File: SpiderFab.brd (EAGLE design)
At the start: 69.8 x 50.8 mm, 47 parts, among them IC1 SN754410, J14 5.5x2.1mm Barrel, U1 ATMEGA328, U3 MCP73831, X1 USBSMD, Y1 16MHz

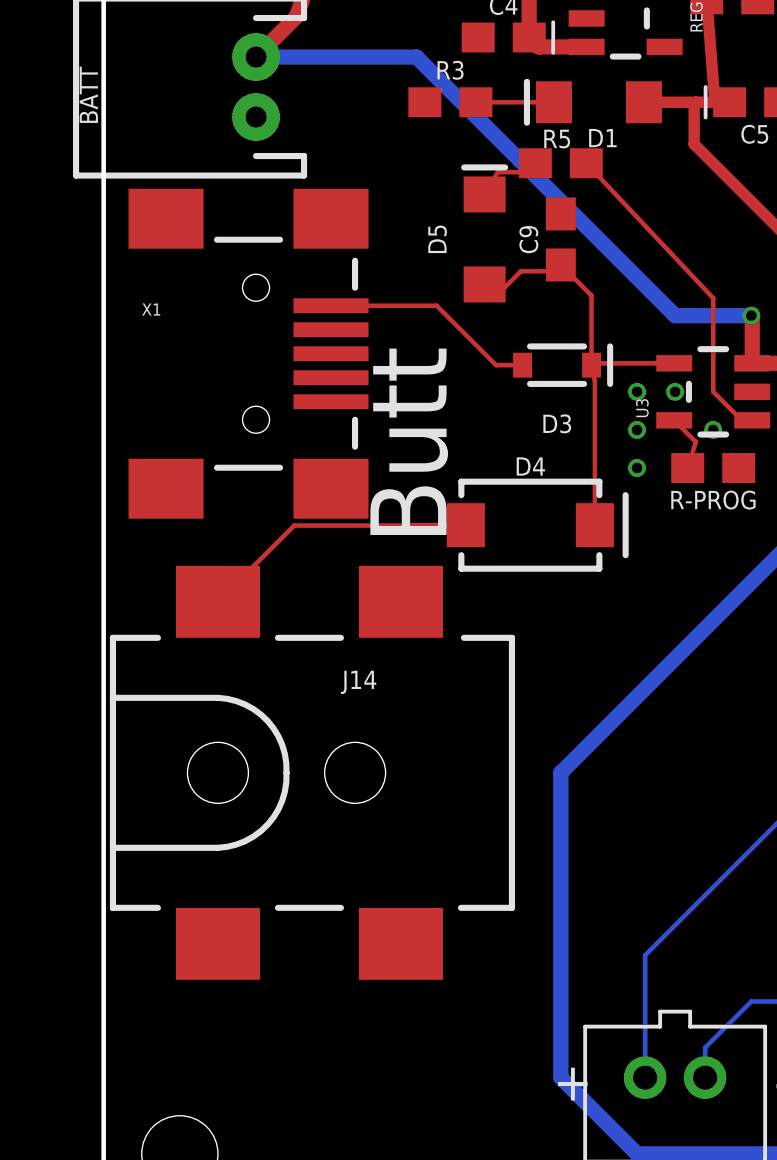
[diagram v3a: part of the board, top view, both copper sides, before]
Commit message: Swap some components for a different package.
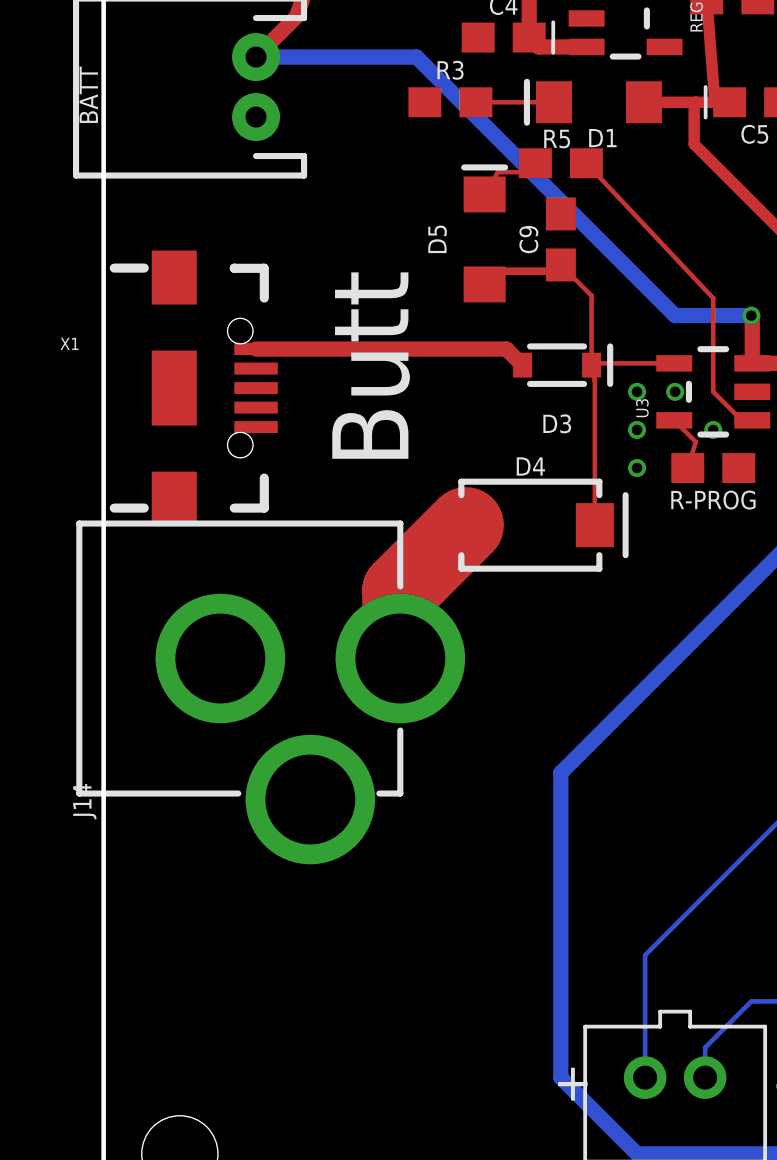
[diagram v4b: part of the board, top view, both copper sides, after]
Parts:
- J14: value 5.5x2.1mm Barrel -> POWER_JACK; device SparkFun-Connectors:POWER_JACK_SMD -> SparkFun-Connectors:POWER_JACK_PTH
- X1: value USBSMD -> AMP FCI 10103594-0001LF; device SparkFun-Connectors:USB-MINIB -> SparkFun-Connectors:USB-B-MICRO-SMD
- moved J14 8.52 mm to (-3.81, 19.1), turned to 270 degrees
- moved X1 2.96 mm to (2.35, 28.1)
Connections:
- net GND: now also J14.GNDBREAK; no longer J14.P$4
- net N$9: now also J14.PWR; no longer J14.VIN0
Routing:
- net N$9: track 9.32 -> 5.35 mm
- net N$8: track 7.20 -> 9.11 mm
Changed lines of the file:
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@@
 <wire x1="65.405" y1="40.64" x2="53.34" y2="40.64" width="0.1524" layer="21"/>
 <text x="58.42" y="31.75" size="2.54" layer="21" rot="R270">Front</text>
-<text x="11.43" y="22.86" size="2.54" layer="21" rot="R90">Butt</text>
+<text x="10.16" y="25.4" size="2.54" layer="21" rot="R90">Butt</text>
 <text x="61.087" y="9.779" size="0.762" layer="21" rot="R180">Front Right Leg</text>
 <text x="49.276" y="9.906" size="0.762" layer="21" rot="R180">Back Right Leg</text>
@@
 <attribute name="VALUE" x="44.45" y="5.588" size="0.6096" layer="27" font="vector" ratio="20"/>
 </element>
-<element name="J14" library="SparkFun-Connectors" library_urn="urn:adsk.eagle:library:513" package="POWER_JACK_SMD" package3d_urn="urn:adsk.eagle:package:38221/1" value="5.5x2.1mm Barrel" x="3.81" y="15.24" smashed="yes">
-<attribute name="NAME" x="7.9502" y="18.034" size="0.6096" layer="25" font="vector" ratio="20"/>
-<attribute name="PROD_ID" value="CONN-08106" x="39.37" y="7.62" size="1.778" layer="27" display="off"/>
-<attribute name="SF_ID" value="PRT-12748" x="39.37" y="7.62" size="1.778" layer="27" display="off"/>
+<element name="J14" library="SparkFun-Connectors" library_urn="urn:adsk.eagle:library:513" package="POWER_JACK_PTH" package3d_urn="urn:adsk.eagle:package:38231/1" value="POWER_JACK" x="-3.81" y="19.05" smashed="yes" rot="R270">
+<attribute name="NAME" x="-1.016" y="14.9098" size="0.6096" layer="25" font="vector" ratio="20" rot="R270"/>
+<attribute name="PROD_ID" value="CONN-08197" x="-11.43" y="-16.51" size="1.778" layer="27" rot="R270" display="off"/>
 </element>
 <element name="FL_A" library="SparkFun-Connectors" library_urn="urn:adsk.eagle:library:513" package="1X03" package3d_urn="urn:adsk.eagle:package:38063/1" value="" x="58.42" y="48.26" smashed="yes">
@@
 <attribute name="VALUE" x="20.5105" y="26.9875" size="0.4064" layer="27" rot="R90"/>
 </element>
-<element name="X1" library="SparkFun-Connectors" package="USB-MINIB" value="USBSMD" x="5.08" y="29.21" smashed="yes">
-<attribute name="NAME" x="1.27" y="30.48" size="0.4064" layer="25"/>
-<attribute name="VALUE" x="1.27" y="29.21" size="0.4064" layer="27"/>
+<element name="X1" library="SparkFun-Connectors" library_urn="urn:adsk.eagle:library:513" package="USB-B-MICRO-SMD" package3d_urn="urn:adsk.eagle:package:38238/1" value="AMP FCI 10103594-0001LF" x="2.355" y="28.065" smashed="yes">
+<attribute name="NAME" x="-1.455" y="29.335" size="0.4064" layer="25"/>
+<attribute name="PROD_ID" value="CONN-11752" x="2.355" y="28.065" size="1.778" layer="27" display="off"/>
 </element>
 <element name="Y1" library="SparkFun-Clocks" library_urn="urn:adsk.eagle:library:511" package="RESONATOR-SMD-3.2X1.3" package3d_urn="urn:adsk.eagle:package:37551/1" value="16MHz" x="50.8" y="30.48" smashed="yes" rot="R90">
@@
 <contactref element="C4" pad="-"/>
 <contactref element="REG1" pad="2"/>
+<contactref element="J14" pad="GNDBREAK"/>
 <contactref element="J14" pad="GND"/>
-<contactref element="J14" pad="P$4"/>
 <contactref element="S1" pad="2"/>
 <contactref element="S1" pad="3"/>
@@
 <wire x1="30.32" y1="38.68" x2="31.75" y2="38.95" width="0.1524" layer="1"/>
 </signal>
-<signal name="N$8">
-<contactref element="X1" pad="VBUS"/>
-<contactref element="D3" pad="A"/>
-<wire x1="7.58" y1="30.81" x2="11.1" y2="30.81" width="0.1524" layer="1"/>
-<wire x1="13.081" y1="28.829" x2="13.963" y2="28.829" width="0.1524" layer="1"/>
-<wire x1="11.1" y1="30.81" x2="13.081" y2="28.829" width="0.1524" layer="1"/>
-</signal>
 <signal name="N$14">
 <contactref element="D3" pad="C"/>
@@
 <wire x1="16.263" y1="28.829" x2="16.41164375" y2="28.89" width="0.1524" layer="1"/>
 <wire x1="16.41164375" y1="28.89" x2="19.0199" y2="28.89" width="0.1524" layer="1"/>
-<wire x1="15.45" y1="31.96" x2="15.24" y2="32.17" width="0.1524" layer="1"/>
-<wire x1="12.7" y1="31.52" x2="12.8928" y2="31.4128" width="0.1524" layer="1"/>
-<wire x1="12.8928" y1="31.4128" x2="13.365725" y2="31.4128" width="0.1524" layer="1"/>
-<wire x1="13.365725" y1="31.4128" x2="13.912925" y2="31.96" width="0.1524" layer="1"/>
-<wire x1="13.912925" y1="31.96" x2="15.45" y2="31.96" width="0.1524" layer="1"/>
-<wire x1="15.24" y1="32.17" x2="16.263" y2="31.147" width="0.1524" layer="1"/>
+<wire x1="15.24" y1="32.17" x2="15.45" y2="31.96" width="0.1524" layer="1"/>
+<wire x1="15.45" y1="31.96" x2="16.263" y2="31.147" width="0.1524" layer="1"/>
 <wire x1="16.263" y1="31.147" x2="16.263" y2="28.829" width="0.1524" layer="1"/>
+<wire x1="12.7" y1="31.52" x2="13.14" y2="31.96" width="0.254" layer="1"/>
+<wire x1="13.14" y1="31.96" x2="15.45" y2="31.96" width="0.254" layer="1"/>
 </signal>
 <signal name="N$15">
@@
 </signal>
 <signal name="N$9">
-<contactref element="J14" pad="VIN0"/>
+<contactref element="J14" pad="PWR"/>
 <contactref element="D4" pad="A"/>
-<wire x1="10.1946875" y1="23.4814" x2="10.2082875" y2="23.495" width="0.1524" layer="1"/>
-<wire x1="10.2082875" y1="23.495" x2="12.074" y2="23.495" width="0.1524" layer="1"/>
-<wire x1="3.81" y1="20.94" x2="6.3514" y2="23.4814" width="0.1524" layer="1"/>
-<wire x1="6.3514" y1="23.4814" x2="10.1946875" y2="23.4814" width="0.1524" layer="1"/>
+<wire x1="9.89" y1="19.05" x2="9.89" y2="21.311" width="2.54" layer="1"/>
+<wire x1="9.89" y1="21.311" x2="12.074" y2="23.495" width="2.54" layer="1"/>
+</signal>
+<signal name="N$8">
+<contactref element="X1" pad="VBUS"/>
+<contactref element="D3" pad="A"/>
+<wire x1="5.08" y1="29.365" x2="13.427" y2="29.365" width="0.508" layer="1"/>
+<wire x1="13.427" y1="29.365" x2="13.963" y2="28.829" width="0.508" layer="1"/>
 </signal>
 </signals>
@@
 <mfgpreviewcolor name="substratecolor" color="0xFF786E46"/>
 </mfgpreviewcolors>
+<errors>
+</errors>
 </board>
 </drawing>
